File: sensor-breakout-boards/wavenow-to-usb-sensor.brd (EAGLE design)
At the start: 24 x 30 mm, 4 parts, among them X1 Type-A Receptacle, X2 Micro Type-B Receptacle

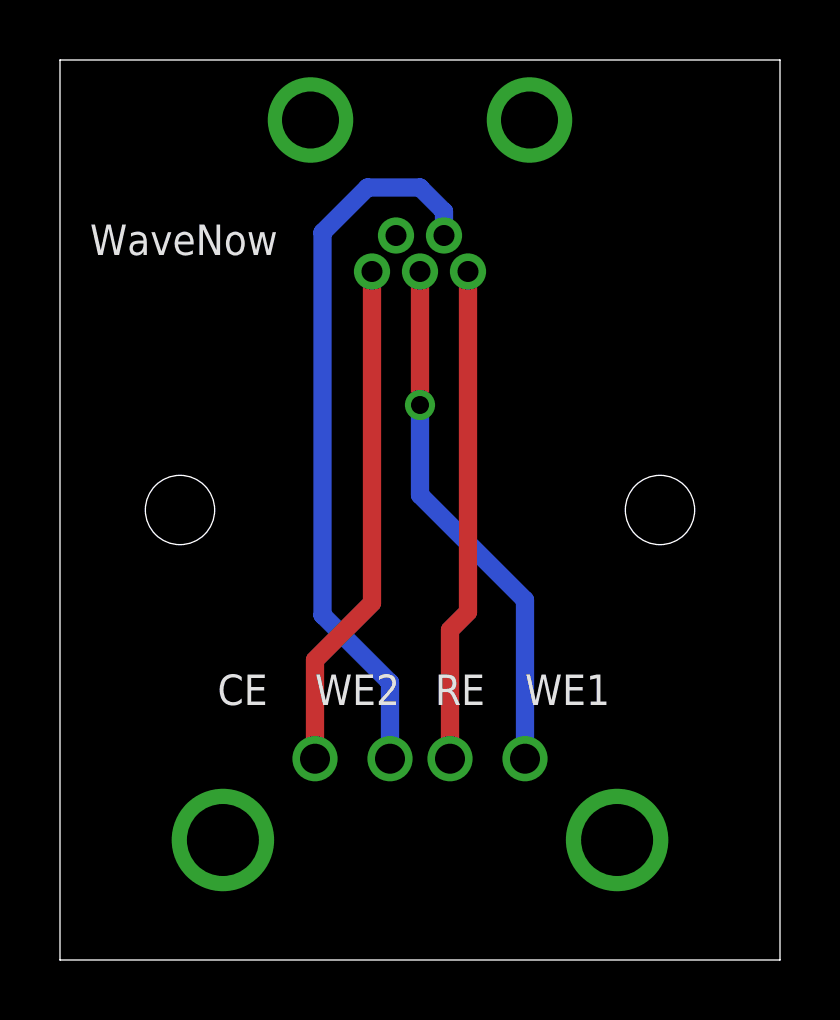
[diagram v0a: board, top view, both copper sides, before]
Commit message: corrected wavenow-to-usb connections
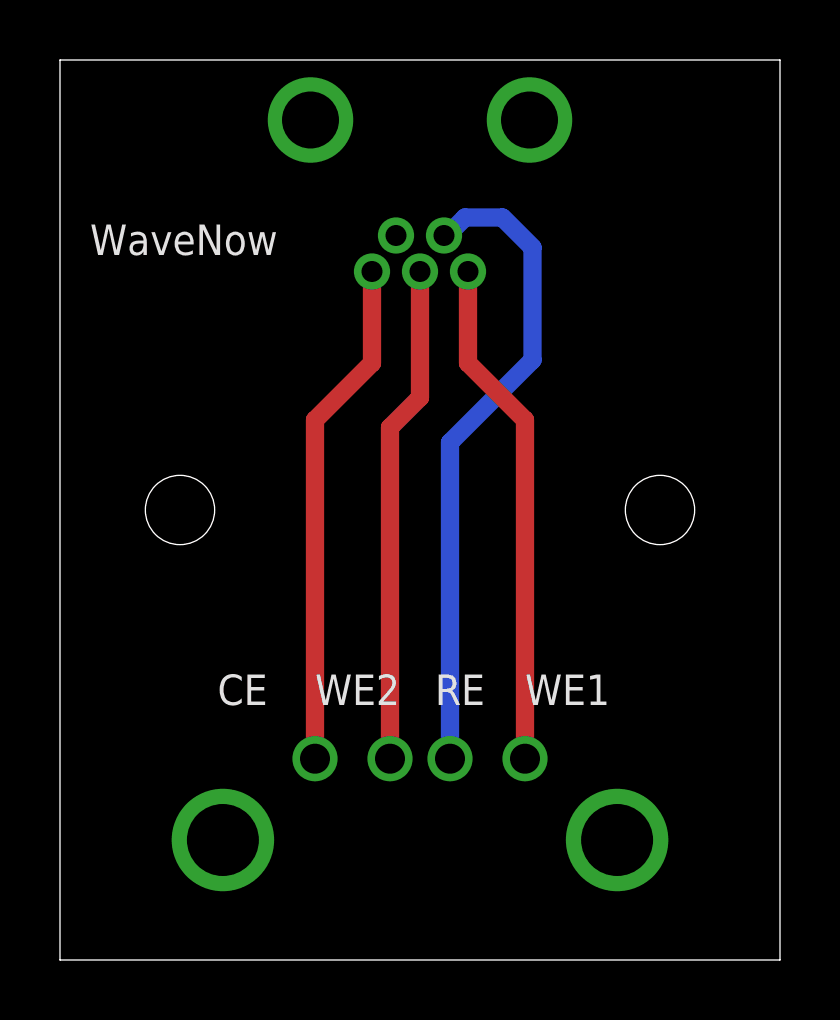
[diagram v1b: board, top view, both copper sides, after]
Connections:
- net RE: now also X2.2; no longer X2.1
- net WE1: now also X2.1; no longer X2.3
- net WE2: now also X2.3; no longer X2.2
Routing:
- net WE2: track 24.3 -> 16.7 mm
- net RE: track 16.5 -> 21.8 mm
- net WE1: track 17.7 -> 17.0 mm, vias 1 -> 0
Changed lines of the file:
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@@
 </elements>
 <signals>
+<signal name="WE1">
+<contactref element="X2" pad="1"/>
+<contactref element="X1" pad="4"/>
+<wire x1="13.6" y1="22.95" x2="13.6" y2="19.9" width="0.6096" layer="1"/>
+<wire x1="13.6" y1="19.9" x2="15.5" y2="18" width="0.6096" layer="1"/>
+<wire x1="15.5" y1="18" x2="15.5" y2="6.71" width="0.6096" layer="1"/>
+</signal>
 <signal name="RE">
-<contactref element="X2" pad="1"/>
+<contactref element="X2" pad="2"/>
 <contactref element="X1" pad="3"/>
-<wire x1="13.6" y1="22.95" x2="13.6" y2="11.6" width="0.6096" layer="1"/>
-<wire x1="13.6" y1="11.6" x2="13" y2="11" width="0.6096" layer="1"/>
-<wire x1="13" y1="11" x2="13" y2="6.71" width="0.6096" layer="1"/>
+<wire x1="12.8" y1="24.15" x2="12.9" y2="24.15" width="0.6096" layer="16"/>
+<wire x1="12.9" y1="24.15" x2="13.5" y2="24.75" width="0.6096" layer="16"/>
+<wire x1="13.5" y1="24.75" x2="14.75" y2="24.75" width="0.6096" layer="16"/>
+<wire x1="14.75" y1="24.75" x2="15.75" y2="23.75" width="0.6096" layer="16"/>
+<wire x1="15.75" y1="23.75" x2="15.75" y2="20" width="0.6096" layer="16"/>
+<wire x1="15.75" y1="20" x2="13" y2="17.25" width="0.6096" layer="16"/>
+<wire x1="13" y1="17.25" x2="13" y2="6.71" width="0.6096" layer="16"/>
 </signal>
 <signal name="WE2">
-<contactref element="X2" pad="2"/>
+<contactref element="X2" pad="3"/>
 <contactref element="X1" pad="2"/>
-<wire x1="12.8" y1="24.15" x2="12.8" y2="24.95" width="0.6096" layer="16"/>
-<wire x1="12.8" y1="24.95" x2="12" y2="25.75" width="0.6096" layer="16"/>
-<wire x1="12" y1="25.75" x2="10.25" y2="25.75" width="0.6096" layer="16"/>
-<wire x1="10.25" y1="25.75" x2="8.75" y2="24.25" width="0.6096" layer="16"/>
-<wire x1="8.75" y1="24.25" x2="8.75" y2="11.5" width="0.6096" layer="16"/>
-<wire x1="8.75" y1="11.5" x2="11" y2="9.25" width="0.6096" layer="16"/>
-<wire x1="11" y1="9.25" x2="11" y2="6.71" width="0.6096" layer="16"/>
-</signal>
-<signal name="WE1">
-<contactref element="X2" pad="3"/>
-<contactref element="X1" pad="4"/>
-<via x="12" y="18.5" extent="1-16" drill="0.6"/>
-<wire x1="12" y1="22.95" x2="12" y2="18.5" width="0.6096" layer="1"/>
-<wire x1="12" y1="18.5" x2="12" y2="15.5" width="0.6096" layer="16"/>
-<wire x1="12" y1="15.5" x2="15.5" y2="12" width="0.6096" layer="16"/>
-<wire x1="15.5" y1="12" x2="15.5" y2="6.71" width="0.6096" layer="16"/>
+<wire x1="12" y1="22.95" x2="12" y2="18.75" width="0.6096" layer="1"/>
+<wire x1="12" y1="18.75" x2="11" y2="17.75" width="0.6096" layer="1"/>
+<wire x1="11" y1="17.75" x2="11" y2="6.71" width="0.6096" layer="1"/>
 </signal>
 <signal name="CE">
 <contactref element="X2" pad="5"/>
 <contactref element="X1" pad="1"/>
-<wire x1="10.4" y1="22.95" x2="10.4" y2="11.9" width="0.6096" layer="1"/>
-<wire x1="10.4" y1="11.9" x2="8.5" y2="10" width="0.6096" layer="1"/>
-<wire x1="8.5" y1="10" x2="8.5" y2="6.71" width="0.6096" layer="1"/>
+<wire x1="10.4" y1="22.95" x2="10.4" y2="19.9" width="0.6096" layer="1"/>
+<wire x1="10.4" y1="19.9" x2="8.5" y2="18" width="0.6096" layer="1"/>
+<wire x1="8.5" y1="18" x2="8.5" y2="6.71" width="0.6096" layer="1"/>
 </signal>
 </signals>
